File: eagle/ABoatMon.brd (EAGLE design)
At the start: 78.7 x 61 mm, 29 parts, among them J1 5V, J2 GND, J3 GND, J4 5V, X1 MKDSN1,5/2-5,08

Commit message: added M0
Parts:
- removed C1: 0.1U, SparkFun-Capacitors:CAP-PTH-SMALL-KIT
- removed J4: 5V, SparkFun-Connectors:1X01
- removed JST1: LIPO, adafruit:JST-PH-2-THM
- removed LIPO: (no value), microbuilder:1X02_ROUND
- removed MOTEINO_MEGA: HEADERS, Moteino:MOTEINO_MEGA_SIMPLE
- removed R2: 1.8M, SparkFun-Resistors:AXIAL-0.3
- removed R3: 3.3M, SparkFun-Resistors:AXIAL-0.3
- added U$6: MOTEINO_M0, Moteino:MOTEINO_M0
- J1: value 5V -> VUSB
- moved R6 67.5 mm to (72.4, 58.4), turned to 180 degrees
- moved VCC 65.9 mm to (63.5, 58.4), turned to 90 degrees
- moved X1 15.2 mm to (5.08, 34.3), turned to 270 degrees
- moved C2 12.8 mm to (5.08, 45.7), turned to 180 degrees
- moved R7 5.08 mm to (50.8, 45.7)
- moved R5 2.54 mm to (6.35, 41.9), turned to 0 degrees
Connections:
- removed net 5V: J1.1, J4.1
- removed net A0: C1.1, MOTEINO_MEGA.A0, R2.P$1, R3.P$2
- removed net A5_VCC_VD: C2.1, MOTEINO_MEGA.A5, R5.P$2, R6.1
- removed net D10_GPS_RX: JP1.5, MOTEINO_MEGA.D10
- removed net D11_GPS_TX: JP1.4, MOTEINO_MEGA.D11
- removed net D12_GPS_ENABLE: JP1.8, MOTEINO_MEGA.D12
- removed net D13_FONA_NETSTAT: FONA.2, MOTEINO_MEGA.D13
- removed net D14_FONA_KEY: FONA.6, MOTEINO_MEGA.D14
- removed net D18_FONA_PS: FONA.7, MOTEINO_MEGA.D18
- removed net D19_PWRON: ENABLE.1, MOTEINO_MEGA.D19
- removed net D25_LED_SWITCH: JST.6, MOTEINO_MEGA.A1
- removed net D26_LED: MOTEINO_MEGA.A2, R7.P$2
- removed net D27_DS_PWR: JST.3, MOTEINO_MEGA.A3, R1.P$1
- removed net D28_DS_DATA: JST.5, MOTEINO_MEGA.A4, R1.P$2
- removed net D8_FONA_TX: FONA.3, MOTEINO_MEGA.D8
- removed net D9_FONA_RX: FONA.4, MOTEINO_MEGA.D9
- removed net VIN: FONA.12, LIPO.1, MOTEINO_MEGA.VIN, MOTEINO_MEGA.VIN_2, R2.P$2
- removed net VIN_JUMPER: JST1.1, LIPO.2
- new net A1_VCC_VD: C2.1, R5.P$2, R6.1, U$6.A1
- new net D0_RX_GPS: JP1.5, U$6.D0_RX1
- new net D10_FONA_KEY: FONA.6, U$6.D10
- new net D11_FONA_PS: FONA.7, U$6.D11
- new net D12_PWRON: ENABLE.1, U$6.D12
- new net D1_TX_GPS: JP1.4, U$6.D1_TX1
- new net D30_TX_FONA: FONA.3, U$6.D30_TX
- new net D31_RX_FONA: FONA.4, U$6.D31_RX
- new net D4_LED: R7.P$2, U$6.D4
- new net D5_LED_SWITCH: JST.6, U$6.D5
- new net D6_DS_PWR: JST.3, R1.P$1, U$6.D6
- new net D7_DS_DATA: JST.5, R1.P$2, U$6.D7
- new net D8_FONA_NETSTAT: FONA.2, U$6.D8
- new net D9_GPS_ENABLE: JP1.8, U$6.D9
- new net VUSB: FONA.12, J1.1, U$6.VUSB
- net 3.3V: now also U$6.3V3, U$6.3V3_2; no longer MOTEINO_MEGA.3V3, MOTEINO_MEGA.3V3_2
- net D3_BILGESW: now also U$6.D3; no longer MOTEINO_MEGA.D3
- net GND: now also U$6.GND, U$6.GND_1, U$6.GND_2; no longer C1.2, JST1.2, MOTEINO_MEGA.GND1, MOTEINO_MEGA.GND_2, R3.P$1
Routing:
- net D0_RX_GPS: track 0.00 -> 139.0 mm, vias 0 -> 6
- net D1_TX_GPS: track 0.00 -> 130.3 mm, vias 0 -> 2
- net VIN: track 117.8 -> 0.00 mm
- net D5_LED_SWITCH: track 0.00 -> 111.6 mm, vias 0 -> 3
- net A1_VCC_VD: track 0.00 -> 91.4 mm, vias 0 -> 1
- net VUSB: track 0.00 -> 85.2 mm
- net D11_GPS_TX: track 83.5 -> 0.00 mm, vias 2 -> 0
- net A0: track 72.4 -> 0.00 mm
- net D27_DS_PWR: track 67.7 -> 0.00 mm, vias 1 -> 0
- net A5_VCC_VD: track 66.8 -> 0.00 mm
- net VCC_JUMPER: track 76.1 -> 9.41 mm
- net D6_DS_PWR: track 0.00 -> 66.0 mm, vias 0 -> 1
- net D18_FONA_PS: track 61.9 -> 0.00 mm, vias 1 -> 0
- net D10_GPS_RX: track 59.5 -> 0.00 mm, vias 2 -> 0
- net D25_LED_SWITCH: track 58.8 -> 0.00 mm, vias 4 -> 0
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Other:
- board text added: "A1_VCC_VD"
- board text added: "D0_GPS_RX"
- board text added: "D0_RX_GPS"
- board text added: "D10_FONA_KEY"
- board text added: "D11_FONA_PS"
- board text added: "D12_PWRON"
- board text added: "D1_GPS_TX"
- board text added: "D1_TX_GPS"
- board text added: "D30_FONA_TX"
- board text added: "D30_TX_FONA"
- board text added: "D31_FONA_RX"
- board text added: "D31_RX_FONA"
- board text added: "D4_LED"
- board text added: "D5_LED_SWITCH"
- board text added: "D6_DS_PWR"
- board text added: "D7_DS_DATA"
- board text added: "D8_FONA_NETSTAT"
- board text added: "D9_GPS_ENABLE"
- board text added: "VUSB"
- board text removed: "A5_VCC_VD"
- board text removed: "AO"
- board text removed: "D10_GPS_RX"
- board text removed: "D11_GPS_TX"
- board text removed: "D12_GPS_ENABLE"
- board text removed: "D13_FONA_NETSTAT"
- board text removed: "D14_FONA_KEY"
- board text removed: "D18_FONA_PS"
- board text removed: "D19_PWRON"
- board text removed: "D25_LED_SWITCH"
- board text removed: "D26_LED"
- board text removed: "D27_DS_PWR"
- board text removed: "D28_DS_DATA"
- board text removed: "D8_FONA_TX"
- board text removed: "D9_FONA_RX"
- board text removed: "VIN LIPO"

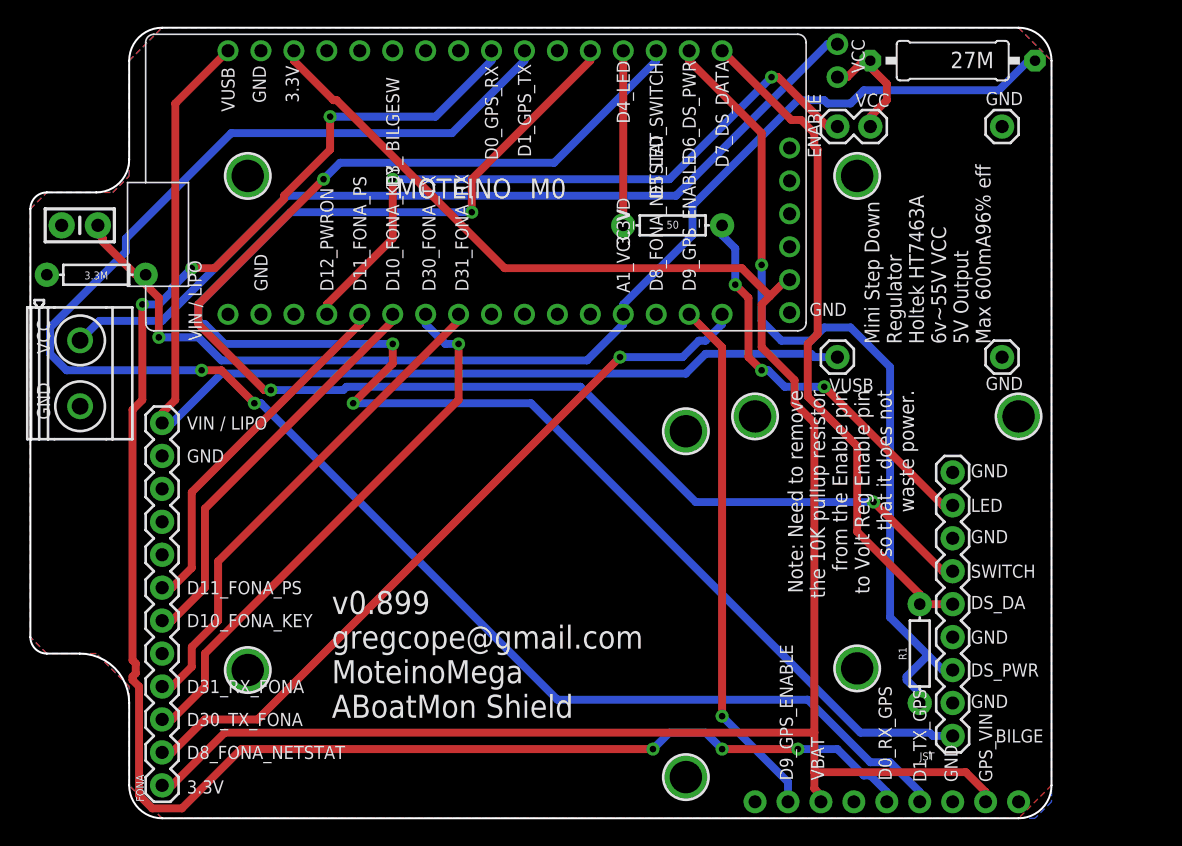
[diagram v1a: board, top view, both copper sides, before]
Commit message: added CAM-M8
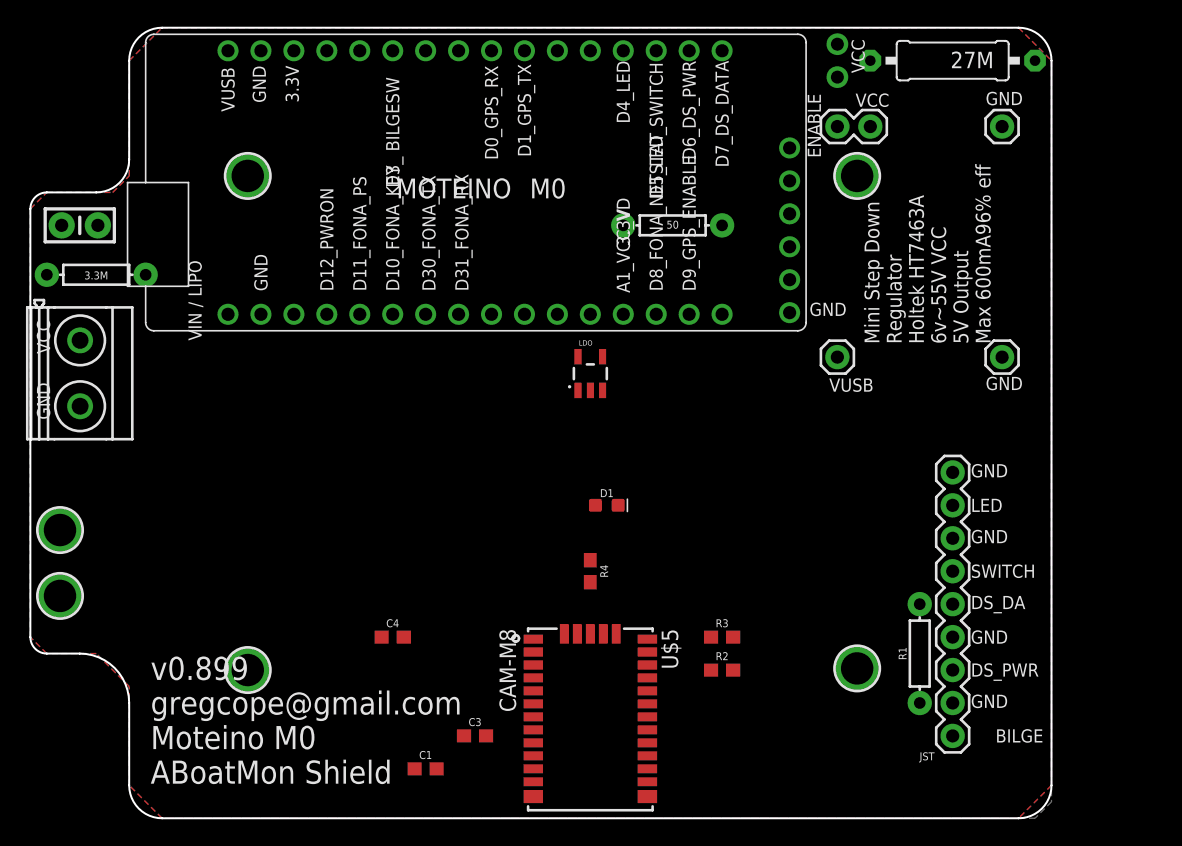
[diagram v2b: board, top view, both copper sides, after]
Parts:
- removed FONA: (no value), SparkFun-Connectors:1X12
- removed JP1: GPS, microbuilder:1X09_ROUND_70
- removed U$3: MOUNTINGHOLE2.5, microbuilder:MOUNTINGHOLE_2.5_PLATED
- added C1, C3: 100nF, SparkFun-Capacitors:0603
- added C4: 4.7uF, SparkFun-Capacitors:0603
- added D1: GREEN, SparkFun-LED:LED-0603
- added LDO: MCP1711T, SparkFun-IC-Power:SOT23-5
- added R2, R3, R4: 220, SparkFun-Resistors:0603
- U$5: value MOUNTINGHOLE2.5 -> CAM-M8; device microbuilder:MOUNTINGHOLE_2.5_PLATED -> ubloxLib:CAM-M8
- moved U$2 51.9 mm to (3.56, 22.2)
- moved U$4 49.9 mm to (3.56, 17.1)
- moved U$5 40.5 mm to (44.5, 7.62), turned to 270 degrees
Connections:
- new net D11_LNA_EN: U$5.30
- new net D12_TIMEPULSE: D1.C
- new net D13_ENABLE: LDO.3
- new net N$1: R4.2, U$5.29
- new net N$2: R2.2, U$5.25
- new net N$3: R3.2, U$5.26
- new net N$4: D1.A, R4.1
- new net N$5: U$5.16, U$5.17
- new net PB22/TXD: R3.1
- new net PB23/RXD: R2.1
- net 3.3V: now also U$5.8; no longer FONA.1, JP1.2, JP1.7
- net D0_RX_GPS: no longer JP1.5
- net D10_FONA_KEY: no longer FONA.6
- net D11_FONA_PS: no longer FONA.7
- net D1_TX_GPS: no longer JP1.4
- net D30_TX_FONA: no longer FONA.3
- net D31_RX_FONA: no longer FONA.4
- net D8_FONA_NETSTAT: no longer FONA.2
- net D9_GPS_ENABLE: no longer JP1.8
- net GND: now also C1.2, C3.2, C4.2, LDO.2, U$5.10, U$5.11, U$5.12, U$5.13, U$5.14, U$5.15, U$5.18, U$5.19, U$5.21, U$5.22, U$5.27, U$5.31, U$5.4, U$5.5; no longer FONA.11, JP1.3
- net VCC: now also C3.1, C4.1, LDO.5, U$5.1, U$5.9
- net VUSB: now also C1.1, LDO.1; no longer FONA.12
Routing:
- net 3.3V: track 154.8 -> 0.00 mm
- net D0_RX_GPS: track 139.0 -> 0.00 mm, vias 6 -> 0
- net D1_TX_GPS: track 130.3 -> 0.00 mm, vias 2 -> 0
- net D3_BILGESW: track 119.9 -> 0.00 mm, vias 3 -> 0
- net D5_LED_SWITCH: track 111.6 -> 0.00 mm, vias 3 -> 0
- net A1_VCC_VD: track 91.4 -> 0.00 mm, vias 1 -> 0
- net VUSB: track 85.2 -> 0.00 mm
- net VCC: track 67.9 -> 0.00 mm
- net D6_DS_PWR: track 66.0 -> 0.00 mm, vias 1 -> 0
- net D8_FONA_NETSTAT: track 57.6 -> 0.00 mm, vias 1 -> 0
- net D7_DS_DATA: track 52.6 -> 0.00 mm
- net D12_PWRON: track 51.6 -> 0.00 mm, vias 2 -> 0
- net D30_TX_FONA: track 42.8 -> 0.00 mm, vias 1 -> 0
- net D9_GPS_ENABLE: track 40.7 -> 0.00 mm, vias 1 -> 0
- net D31_RX_FONA: track 38.6 -> 0.00 mm
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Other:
- board text added: "v0.899 gregcope@gmail.com Moteino M0 ABoatMon Shield"
- board text removed: "D0_RX_GPS"
- board text removed: "D1_TX_GPS"
- board text removed: "D30_TX_FONA"
- board text removed: "D31_RX_FONA"
- board text removed: "GPS_VIN"
- board text removed: "Note: Need to remove the 10K pullup resistor from the Enable pin to Volt Reg Enable pin so that it does not waste power."
- board text removed: "VBAT"
- board text removed: "v0.899 gregcope@gmail.com MoteinoMega ABoatMon Shield"

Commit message: started adding nets
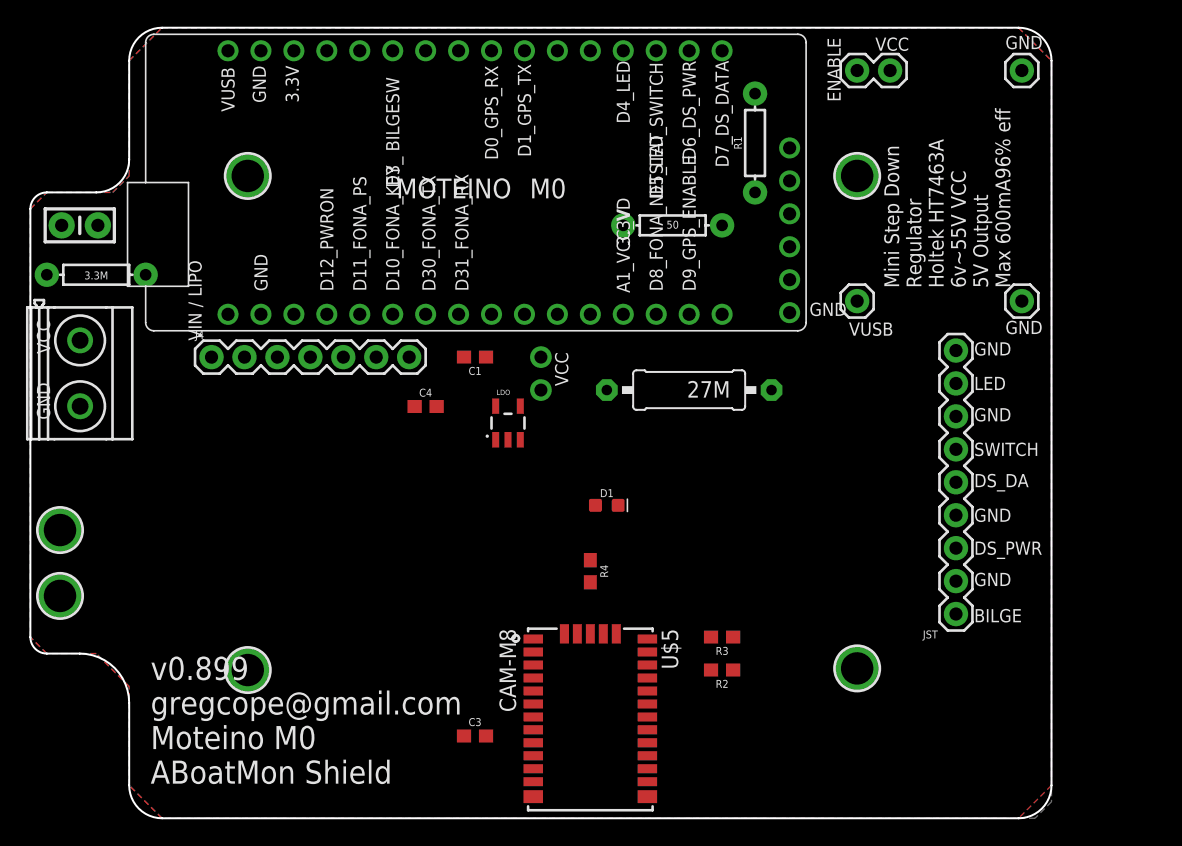
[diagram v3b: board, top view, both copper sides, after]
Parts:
- added J4: (no value), SparkFun-Connectors:1X07
- moved R1 41.4 mm to (57.1, 52.1)
- moved VCC 33.2 mm to (40.6, 34.3)
- moved R6 32.5 mm to (52.1, 33.0)
- moved C1 32.0 mm to (35.6, 35.6), turned to 180 degrees
- moved C4 18.0 mm to (31.8, 31.8)
- moved JST 9.40 mm to (72.6, 15.7)
- moved LDO 7.41 mm to (38.1, 30.5)
- moved ENABLE 4.58 mm to (65.0, 57.7)
- moved J1 4.58 mm to (65.0, 39.9)
- moved J2 4.58 mm to (77.7, 39.9)
- moved J3 4.58 mm to (77.7, 57.7)
- turned R2 to 180 degrees
- turned R3 to 180 degrees
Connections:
- net D12_PWRON renamed D12_VCC_PWRON
- removed net D0_RX_GPS: U$6.D0_RX1
- removed net D10_FONA_KEY: U$6.D10
- removed net D11_FONA_PS: U$6.D11
- removed net D11_LNA_EN: U$5.30
- removed net D13_ENABLE: LDO.3
- removed net D1_TX_GPS: U$6.D1_TX1
- removed net D30_TX_FONA: U$6.D30_TX
- removed net D31_RX_FONA: U$6.D31_RX
- removed net D8_FONA_NETSTAT: U$6.D8
- removed net D9_GPS_ENABLE: U$6.D9
- removed net PB22/TXD: R3.1
- removed net PB23/RXD: R2.1
- new net D0_RX_GNS: R2.1, U$6.D0_RX1
- new net D10_7020_SLEEP: J4.7, U$6.D10
- new net D11_7020_PWRKEY: J4.4, U$6.D11
- new net D1_TX_GNS: R3.1, U$6.D1_TX1
- new net D30_TX_7020: J4.2, U$6.D30_TX
- new net D31_RX_7020: J4.3, U$6.D31_RX
- new net D8_LNA_EN: U$5.30, U$6.D8
- new net D9_GNS_ENABLE: LDO.3, U$6.D9
- new net GNS_VCC: C3.1, C4.1, LDO.5, U$5.1, U$5.9
- net GND: now also J4.1, J4.6
- net VCC: no longer C3.1, C4.1, LDO.5, U$5.1, U$5.9
- net VUSB: now also J4.5

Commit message: moved M0 and regulator
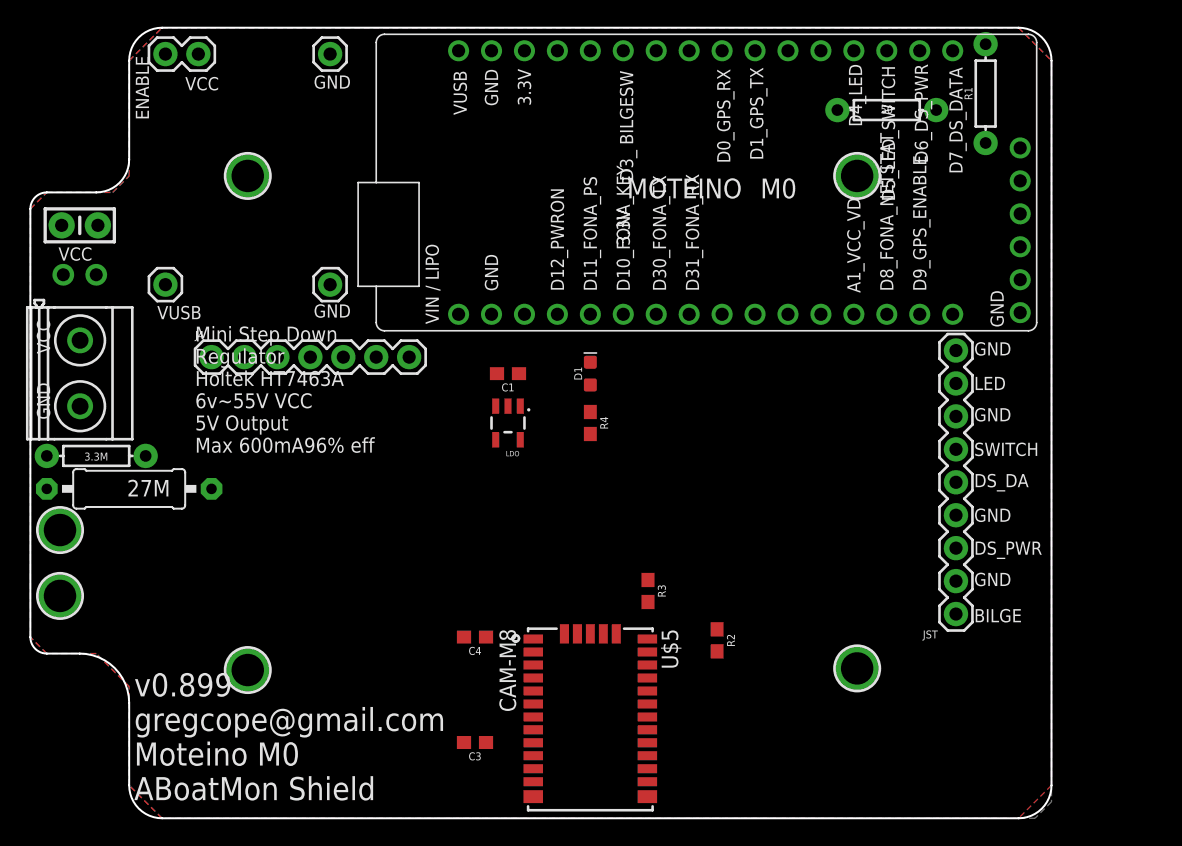
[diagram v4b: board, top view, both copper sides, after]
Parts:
- moved ENABLE 53.4 mm to (11.7, 58.9)
- moved J1 53.4 mm to (11.7, 41.1)
- moved J2 53.4 mm to (24.4, 41.1)
- moved J3 53.4 mm to (24.4, 58.9)
- moved R6 43.8 mm to (8.89, 25.4)
- moved VCC 36.4 mm to (5.08, 41.9), turned to 180 degrees
- moved R7 18.8 mm to (67.3, 54.6)
- moved R1 18.2 mm to (74.9, 55.9)
- moved C4 18.2 mm to (35.6, 14.0), turned to 180 degrees
- moved U$6 17.8 mm to (27.9, 36.8)
- moved R5 14.0 mm to (6.35, 27.9)
- moved R4 11.4 mm to (44.5, 30.5)
- moved D1 10.2 mm to (44.5, 34.3), turned to 90 degrees
- moved R3 6.73 mm to (48.9, 17.5), turned to 270 degrees
- moved C1 2.84 mm to (38.1, 34.3)
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
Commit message: changed nets for gns
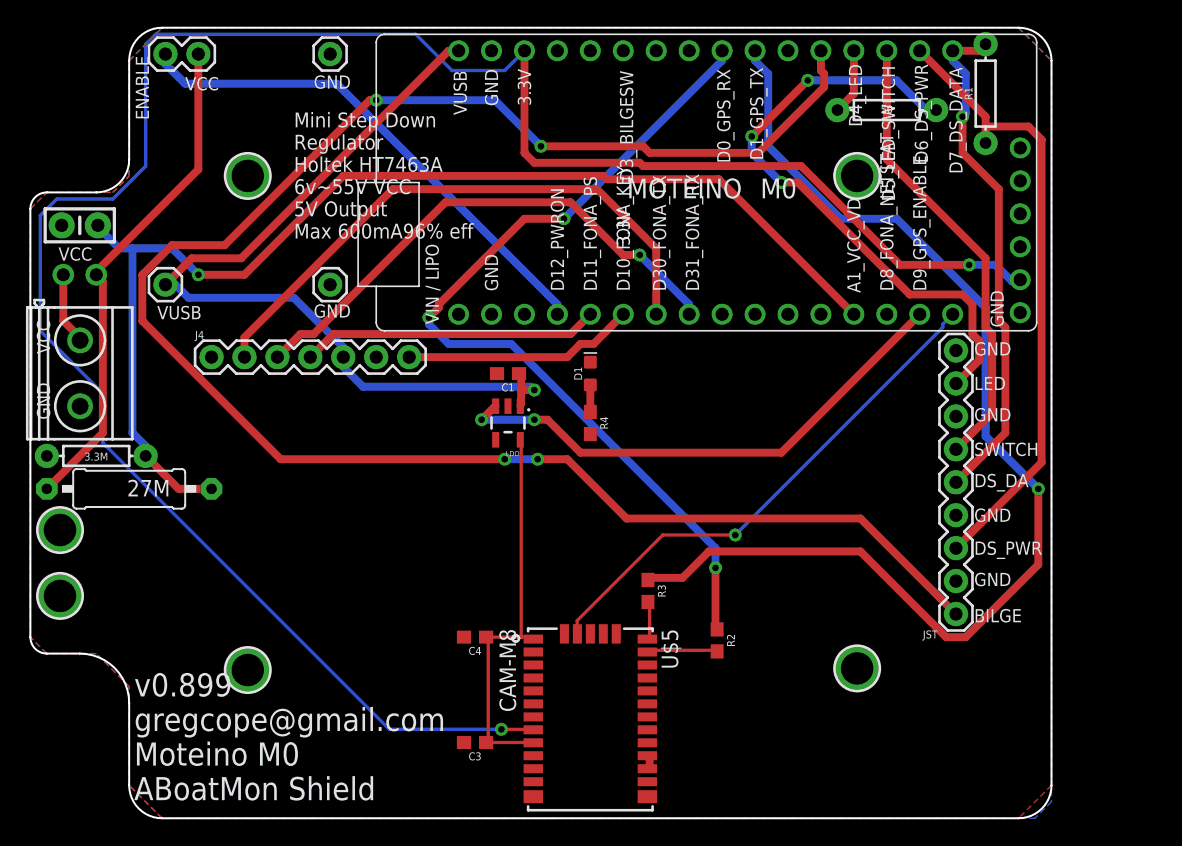
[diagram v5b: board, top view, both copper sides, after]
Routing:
- net 3.3V: track 0.00 -> 162.5 mm, vias 0 -> 2
- net D3_BILGESW: track 0.00 -> 140.5 mm, vias 0 -> 4
- net A1_VCC_VD: track 0.00 -> 90.3 mm, vias 0 -> 1
- net D1_TX_GNS: track 0.00 -> 87.3 mm, vias 0 -> 1
- net D0_RX_GNS: track 0.00 -> 67.8 mm, vias 0 -> 3
- net VUSB: track 0.00 -> 66.5 mm, vias 0 -> 1
- net D6_DS_PWR: track 0.00 -> 48.2 mm
- net LED: track 0.00 -> 47.1 mm, vias 0 -> 3
- net D30_TX_7020: track 0.00 -> 45.0 mm
- net D9_GNS_ENABLE: track 0.00 -> 40.8 mm, vias 0 -> 2
- net D31_RX_7020: track 0.00 -> 40.7 mm, vias 0 -> 1
- net D8_LNA_EN: track 0.00 -> 39.9 mm, vias 0 -> 1
- net D7_DS_DATA: track 0.00 -> 39.5 mm, vias 0 -> 1
- net D12_VCC_PWRON: track 0.00 -> 39.4 mm
- net VCC_JUMPER: track 0.00 -> 38.8 mm
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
